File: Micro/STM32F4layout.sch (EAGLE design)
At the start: 12 parts

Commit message: Next Step for Power, tied I2C high
Next step in micro board schematic
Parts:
- removed C1: (no value), SparkFun-Passives:CAP0603-CAP
- added R1, R2: (no value), SparkFun-Passives:RESISTOR0603-RES
- added R3, R4: 4.7K, SparkFun-Passives:RESISTOR0603-RES
- added U$2, U$3: SWITCH, DiscreteComponents:SWITCH
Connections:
- new net I2C_SCL: R3.1, U$1G$1.PA8
- new net I2C_SDA: R4.1, U$1G$3.PC9
- new net N$3: R1.2, U$1G$6.BOOT0, U$3.P$2
- new net N$4: R2.2, U$1G$6.NRST, U$2.P$2
- net +3V3: now also R2.1, R3.2, R4.2, U$1G$6.VREF+, U$3.P$1
- net GND: now also R1.1, U$1G$6.VSSA, U$2.P$1
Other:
- moved on the sheet: C11, C13, C14, C2, C3, C4

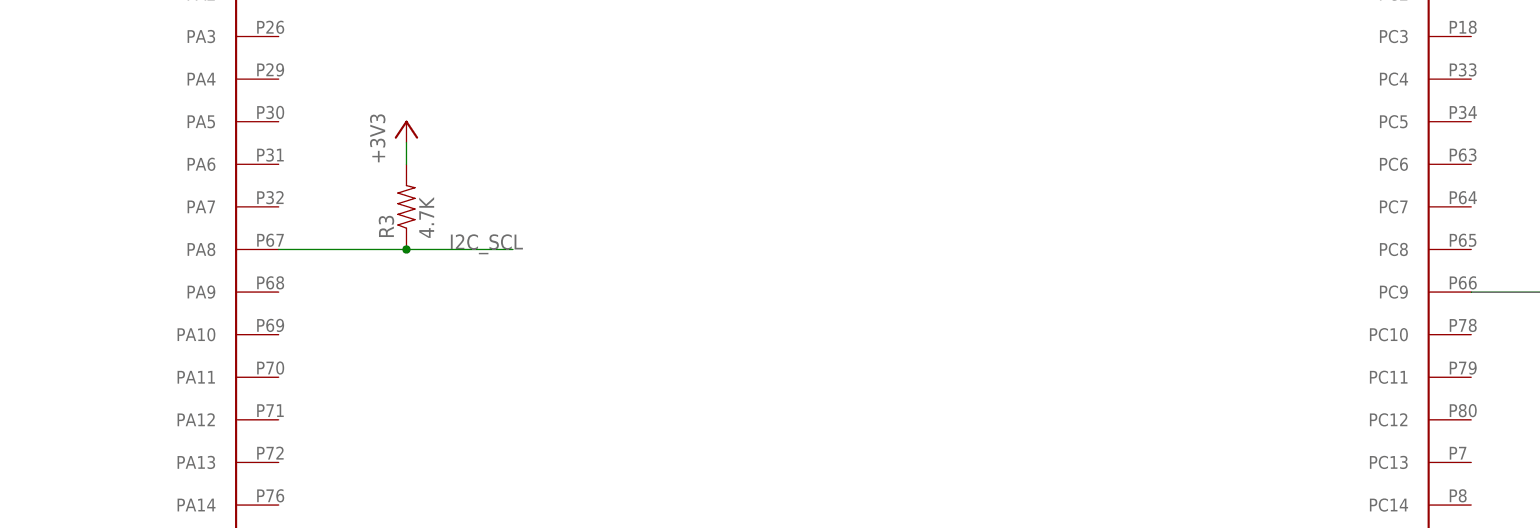
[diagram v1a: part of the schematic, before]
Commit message: Pushed latest updates
Added labels and buttons for boot and such
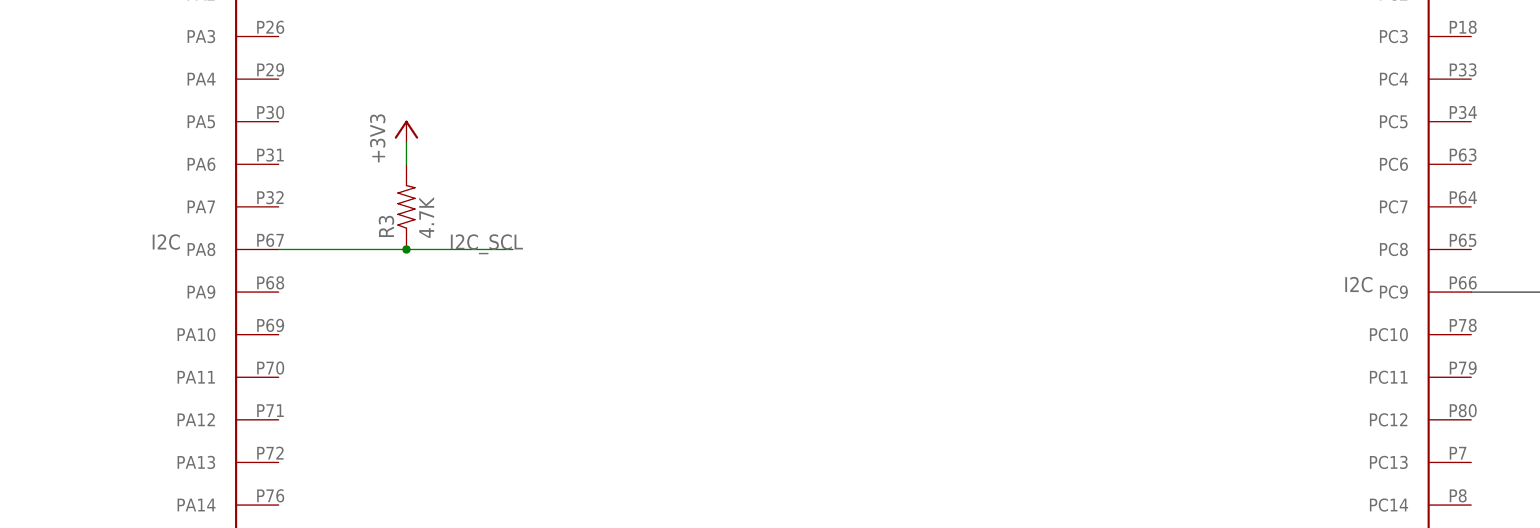
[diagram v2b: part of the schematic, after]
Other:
- note added: "I2C"
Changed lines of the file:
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@@
 <sheet>
 <plain>
+<text x="-86.36" y="78.74" size="1.778" layer="95">I2C</text>
+<text x="55.88" y="73.66" size="1.778" layer="95">I2C</text>
 </plain>
 <instances>

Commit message: Update on more parts
Whooo Updates
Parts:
- removed C3: (no value), SparkFun-Passives:CAP0603-CAP
- added C1: (no value), SparkFun-Passives:CAP0603-CAP
- added D1: (no value), DiscreteComponents:DIODE-DO-214AC
- added Q1: ASF, DiscreteComponents:ASF
- added RN1: (no value), DiscreteComponents:2R-NEXBV4V
- added T1: (no value), DiscreteComponents:FDN340P
- added U$4: MICROUSB, Other:MICROUSB
- added U1: LM1085IS-3.3, PowerComponents:LM1085IS-3.3
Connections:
- new net +5V: D1.A, T1.G
- new net N$10: T1.D, U$4.VCC
- new net N$12: C1.1, Q1.VCC
- new net N$5: D1.C, T1.S
- new net N$6: RN1B.1, U$4.D+
- new net N$7: RN1A.1, U$4.D-
- new net N$8: RN1A.2
- new net N$9: RN1B.2
- new net OSC_IN: Q1.FO, U$1G$5.PH0
- net GND: now also C1.2, Q1.GND, U$4.GND, U$4.ID; no longer C2.2, C3.2
- net N$2: now also C2.2; no longer C3.1
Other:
- note added: "USB_D+"
- note added: "USB_D-"
- moved on the sheet: C2
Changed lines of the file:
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@@
 <part name="U$1" library="Other" deviceset="STM32F4" device=""/>
 <part name="C2" library="SparkFun-Passives" deviceset="CAP" device="0603-CAP"/>
-<part name="C3" library="SparkFun-Passives" deviceset="CAP" device="0603-CAP"/>
-<part name="GND1" library="supply1" deviceset="GND" device=""/>
 <part name="GND2" library="supply1" deviceset="GND" device=""/>
 <part name="C4" library="SparkFun-Passives" deviceset="CAP" device="0603-CAP"/>
@@
 <part name="+3V6" library="supply1" deviceset="+3V3" device=""/>
 <part name="R4" library="SparkFun-Passives" deviceset="RESISTOR" device="0603-RES" value="4.7K"/>
+<part name="Q1" library="DiscreteComponents" deviceset="ASF*" device=""/>
+<part name="T1" library="DiscreteComponents" deviceset="FDN340P" device=""/>
+<part name="FRAME1" library="frames" deviceset="A3L-LOC" device=""/>
+<part name="FRAME2" library="frames" deviceset="A3L-LOC" device=""/>
+<part name="FRAME3" library="frames" deviceset="A3L-LOC" device=""/>
+<part name="FRAME4" library="frames" deviceset="A3L-LOC" device=""/>
+<part name="U$4" library="Other" deviceset="MICROUSB" device=""/>
+<part name="RN1" library="DiscreteComponents" deviceset="2R-N" device="EXBV4V"/>
+<part name="GND7" library="supply1" deviceset="GND" device=""/>
+<part name="P+2" library="supply1" deviceset="+5V" device=""/>
+<part name="D1" library="DiscreteComponents" deviceset="DIODE-" device="DO-214AC"/>
+<part name="C1" library="SparkFun-Passives" deviceset="CAP" device="0603-CAP"/>
+<part name="+3V7" library="supply1" deviceset="+3V3" device=""/>
+<part name="GND10" library="supply1" deviceset="GND" device=""/>
+<part name="U1" library="PowerComponents" deviceset="LM1085IS-3.3" device=""/>
 </parts>
 <sheets>
@@
 <text x="-86.36" y="78.74" size="1.778" layer="95">I2C</text>
 <text x="55.88" y="73.66" size="1.778" layer="95">I2C</text>
+<text x="-454.66" y="-279.4" size="1.778" layer="95">USB_D+</text>
+<text x="-454.66" y="-269.24" size="1.778" layer="95">USB_D-</text>
 </plain>
 <instances>
@@
 <instance part="U$1" gate="G$5" x="193.04" y="-2.54"/>
 <instance part="U$1" gate="G$6" x="-284.48" y="2.54"/>
-<instance part="C2" gate="G$1" x="-378.46" y="-17.78"/>
-<instance part="C3" gate="G$1" x="-370.84" y="-17.78"/>
-<instance part="GND1" gate="1" x="-374.142" y="-25.4"/>
+<instance part="C2" gate="G$1" x="-337.82" y="-7.62"/>
 <instance part="GND2" gate="1" x="-317.5" y="5.588"/>
 <instance part="C4" gate="G$1" x="-248.92" y="0"/>
@@
 <instance part="+3V6" gate="G$1" x="88.9" y="88.9"/>
 <instance part="R4" gate="G$1" x="88.9" y="78.74" rot="R90"/>
+<instance part="Q1" gate="G$1" x="-73.66" y="-160.02"/>
+<instance part="T1" gate="A" x="-477.52" y="-259.08" rot="R180"/>
+<instance part="FRAME1" gate="G$1" x="-121.92" y="-129.54"/>
+<instance part="FRAME2" gate="G$1" x="-510.54" y="-129.54"/>
+<instance part="FRAME3" gate="G$1" x="-510.54" y="-391.16"/>
+<instance part="FRAME4" gate="G$1" x="-121.92" y="-391.16"/>
+<instance part="U$4" gate="G$1" x="-492.76" y="-274.32"/>
+<instance part="RN1" gate="A" x="-459.74" y="-271.78"/>
+<instance part="RN1" gate="B" x="-459.74" y="-276.86"/>
+<instance part="GND7" gate="1" x="-480.06" y="-286.766"/>
+<instance part="P+2" gate="1" x="-464.82" y="-243.84"/>
+<instance part="D1" gate="G$1" x="-469.9" y="-251.46" rot="R180"/>
+<instance part="C1" gate="G$1" x="-93.98" y="-160.02"/>
+<instance part="+3V7" gate="G$1" x="-94.234" y="-140.97" smashed="yes">
+<attribute name="VALUE" x="-95.25" y="-139.954" size="1.778" layer="96" rot="R180"/>
+</instance>
+<instance part="GND10" gate="1" x="-93.98" y="-167.64"/>
+<instance part="U1" gate="A" x="-419.1" y="-243.84"/>
 </instances>
 <busses>
 </busses>
 <nets>
-<net name="N$1" class="0">
-<segment>
-<pinref part="U$1" gate="G$6" pin="VCAP_1"/>
-<pinref part="C2" gate="G$1" pin="1"/>
-<wire x1="-307.34" y1="-5.08" x2="-378.46" y2="-5.08" width="0.1524" layer="91"/>
-<wire x1="-378.46" y1="-5.08" x2="-378.46" y2="-12.7" width="0.1524" layer="91"/>
-</segment>
-</net>
-<net name="N$2" class="0">
-<segment>
-<pinref part="U$1" gate="G$6" pin="VCAP_2"/>
-<pinref part="C3" gate="G$1" pin="1"/>
-<wire x1="-307.34" y1="-10.16" x2="-370.84" y2="-10.16" width="0.1524" layer="91"/>
-<wire x1="-370.84" y1="-10.16" x2="-370.84" y2="-12.7" width="0.1524" layer="91"/>
-</segment>
-</net>
 <net name="GND" class="0">
-<segment>
-<pinref part="C3" gate="G$1" pin="2"/>
-<pinref part="C2" gate="G$1" pin="2"/>
-<wire x1="-370.84" y1="-20.32" x2="-374.142" y2="-20.32" width="0.1524" layer="91"/>
-<wire x1="-374.142" y1="-20.32" x2="-378.46" y2="-20.32" width="0.1524" layer="91"/>
-<wire x1="-374.142" y1="-20.32" x2="-374.142" y2="-22.86" width="0.1524" layer="91"/>
-<pinref part="GND1" gate="1" pin="GND"/>
-<wire x1="-374.142" y1="-22.86" x2="-374.142" y2="-23.368" width="0.1524" layer="91"/>
-<junction x="-374.142" y="-22.86"/>
-</segment>
 <segment>
 <pinref part="U$1" gate="G$6" pin="VSS4"/>
@@
 <wire x1="-327.66" y1="-27.94" x2="-327.66" y2="-30.48" width="0.1524" layer="91"/>
 <junction x="-327.66" y="-30.48"/>
+</segment>
+<segment>
+<pinref part="U$4" gate="G$1" pin="GND"/>
+<wire x1="-485.14" y1="-279.4" x2="-480.06" y2="-279.4" width="0.1524" layer="91"/>
+<wire x1="-480.06" y1="-279.4" x2="-480.06" y2="-284.226" width="0.1524" layer="91"/>
+<pinref part="U$4" gate="G$1" pin="ID"/>
+<wire x1="-480.06" y1="-284.226" x2="-480.06" y2="-284.48" width="0.1524" layer="91"/>
+<wire x1="-485.14" y1="-276.86" x2="-480.06" y2="-276.86" width="0.1524" layer="91"/>
+<wire x1="-480.06" y1="-276.86" x2="-480.06" y2="-279.4" width="0.1524" layer="91"/>
+<junction x="-480.06" y="-279.4"/>
+<pinref part="GND7" gate="1" pin="GND"/>
+<junction x="-480.06" y="-284.226"/>
+</segment>
+<segment>
+<pinref part="C1" gate="G$1" pin="2"/>
+<pinref part="Q1" gate="G$1" pin="GND"/>
+<wire x1="-93.98" y1="-165.1" x2="-93.98" y2="-162.56" width="0.1524" layer="91"/>
+<wire x1="-86.36" y1="-165.1" x2="-93.98" y2="-165.1" width="0.1524" layer="91"/>
+<junction x="-93.98" y="-165.1"/>
+<pinref part="GND10" gate="1" pin="GND"/>
+<junction x="-93.98" y="-165.1"/>
 </segment>
 </net>
@@
 </segment>
 </net>
+<net name="N$6" class="0">
+<segment>
+<pinref part="U$4" gate="G$1" pin="D+"/>
+<pinref part="RN1" gate="B" pin="1"/>
+<wire x1="-485.14" y1="-274.32" x2="-464.82" y2="-274.32" width="0.1524" layer="91"/>
+<wire x1="-464.82" y1="-274.32" x2="-464.82" y2="-276.86" width="0.1524" layer="91"/>
+</segment>
+</net>
+<net name="N$7" class="0">
+<segment>
+<pinref part="U$4" gate="G$1" pin="D-"/>
+<pinref part="RN1" gate="A" pin="1"/>
+<wire x1="-485.14" y1="-271.78" x2="-464.82" y2="-271.78" width="0.1524" layer="91"/>
+</segment>
+</net>
+<net name="N$8" class="0">
+<segment>
+<pinref part="RN1" gate="A" pin="2"/>
+<wire x1="-454.66" y1="-271.78" x2="-452.12" y2="-271.78" width="0.1524" layer="91"/>
+</segment>
+</net>
+<net name="N$9" class="0">
+<segment>
+<pinref part="RN1" gate="B" pin="2"/>
+<wire x1="-454.66" y1="-276.86" x2="-452.12" y2="-276.86" width="0.1524" layer="91"/>
+</segment>
+</net>
+<net name="N$10" class="0">
+<segment>
+<pinref part="U$4" gate="G$1" pin="VCC"/>
+<pinref part="T1" gate="A" pin="D"/>
+<wire x1="-485.14" y1="-269.24" x2="-477.52" y2="-269.24" width="0.1524" layer="91"/>
+<wire x1="-477.52" y1="-269.24" x2="-477.52" y2="-264.16" width="0.1524" layer="91"/>
+</segment>
+</net>
+<net name="+5V" class="0">
+<segment>
+<pinref part="T1" gate="A" pin="G"/>
+<wire x1="-472.44" y1="-256.54" x2="-464.82" y2="-256.54" width="0.1524" layer="91"/>
+<wire x1="-464.82" y1="-256.54" x2="-464.82" y2="-251.46" width="0.1524" layer="91"/>
+<pinref part="P+2" gate="1" pin="+5V"/>
+<pinref part="D1" gate="G$1" pin="A"/>
+<wire x1="-464.82" y1="-251.46" x2="-464.82" y2="-246.38" width="0.1524" layer="91"/>
+<wire x1="-464.82" y1="-251.46" x2="-467.36" y2="-251.46" width="0.1524" layer="91"/>
+<junction x="-464.82" y="-251.46"/>
+</segment>
+</net>
+<net name="N$5" class="0">
+<segment>
+<pinref part="D1" gate="G$1" pin="C"/>
+<pinref part="T1" gate="A" pin="S"/>
+<wire x1="-472.44" y1="-251.46" x2="-477.52" y2="-251.46" width="0.1524" layer="91"/>
+<wire x1="-477.52" y1="-251.46" x2="-477.52" y2="-254" width="0.1524" layer="91"/>
+</segment>
+</net>
+<net name="N$12" class="0">
+<segment>
+<pinref part="C1" gate="G$1" pin="1"/>
+<wire x1="-93.98" y1="-154.94" x2="-94.234" y2="-154.94" width="0.1524" layer="91"/>
+<wire x1="-94.234" y1="-154.94" x2="-94.234" y2="-143.256" width="0.1524" layer="91"/>
+<pinref part="Q1" gate="G$1" pin="VCC"/>
+<wire x1="-86.36" y1="-154.94" x2="-93.98" y2="-154.94" width="0.1524" layer="91"/>
+<junction x="-93.98" y="-154.94"/>
+</segment>
+</net>
+<net name="OSC_IN" class="0">
+<segment>
+<pinref part="U$1" gate="G$5" pin="PH0"/>
+<wire x1="208.28" y1="-38.1" x2="213.36" y2="-38.1" width="0.1524" layer="91"/>
+<label x="210.82" y="-38.1" size="1.778" layer="95"/>
+</segment>
+<segment>
+<pinref part="Q1" gate="G$1" pin="FO"/>
+<wire x1="-60.96" y1="-160.02" x2="-43.18" y2="-160.02" width="0.1524" layer="91"/>
+<label x="-55.88" y="-160.02" size="1.778" layer="95"/>
+</segment>
+</net>
+<net name="N$1" class="0">
+<segment>
+<pinref part="C2" gate="G$1" pin="1"/>
+<pinref part="U$1" gate="G$6" pin="VCAP_1"/>
+<wire x1="-337.82" y1="-2.54" x2="-307.34" y2="-2.54" width="0.1524" layer="91"/>
+<wire x1="-307.34" y1="-2.54" x2="-307.34" y2="-5.08" width="0.1524" layer="91"/>
+</segment>
+</net>
+<net name="N$2" class="0">
+<segment>
+<pinref part="U$1" gate="G$6" pin="VCAP_2"/>
+<pinref part="C2" gate="G$1" pin="2"/>
+<wire x1="-307.34" y1="-10.16" x2="-337.82" y2="-10.16" width="0.1524" layer="91"/>
+</segment>
+</net>

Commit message: Worked on List that Luke and I worked on
Includes, almost set up USB, LEDs, Almost a power Supply, CAN Chip
Connections and More!
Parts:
- added C3, C5: 1 uF, capacitor-wima:C2,5-3
- added D2, D3, D4, D5: (no value), SparkFun-LED:LED0603
- added R5, R7: 120, resistor:R-US_0204/2V
- added R6, R8: 100k, resistor:R-US_0204/2V
- added SV1, SV2, SV3: (no value), Connectors:FE18-2
- added U$5, U$6: MAX3051MAX3051, MAX3051 Library:MAX3051MAX3051
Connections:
- new net CAN1_H: R5.1, U$5.CANH
- new net CAN1_L: R5.2, U$5.CANL
- new net CAN1_RX: U$1G$1.PA11, U$5.RXD
- new net CAN1_TX: U$1G$1.PA12, U$5.TXD
- new net CAN2_RX: U$1G$2.PB5, U$6.RXD
- new net CAN2_TX: U$1G$2.PB6, U$6.TXD
- new net CANH1: R7.1, U$6.CANH
- new net CANL1: R7.2, U$6.CANL
- new net ETC_MDC: U$1G$3.PC1
- new net ETH_CRS_DV: U$1G$1.PA7
- new net ETH_MDIO: U$1G$1.PA2
- new net ETH_REF_CLK: U$1G$1.PA1
- new net ETH_RXD0: U$1G$3.PC4
- new net ETH_RXD1: U$1G$3.PC5
- new net ETH_TXD0: U$1G$2.PB12
- new net ETH_TXD1: U$1G$2.PB13
- new net ETH_TX_EN: U$1G$2.PB11
- new net N$11: R6.1, U$5.RS
- new net N$13: R8.1, U$6.RS
- new net N$14: D2.A, U$1G$4.PD11
- new net N$15: D3.A, U$1G$4.PD12
- new net N$16: D4.A, U$1G$4.PD13
- new net N$17: D5.A, U$1G$4.PD14
- new net VCC: C3.2, C5.2, U$5.VCC, U$6.VCC
- net +5V: now also U1.IN
- net GND: now also C3.1, C5.1, D2.C, D3.C, D4.C, D5.C, R6.2, R8.2, U$5.GND, U$6.GND
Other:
- moved on the sheet: R3
